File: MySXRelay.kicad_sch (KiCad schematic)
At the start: 53 parts, among them K1 FH44L-1AT-L1-DC5V, Q1 2N7002, U1 MIC4427, U2 BL0942, U3 BP2525X, U4 Si8642BB-B-IS1, U5 MCP1703Ax-180xxTT

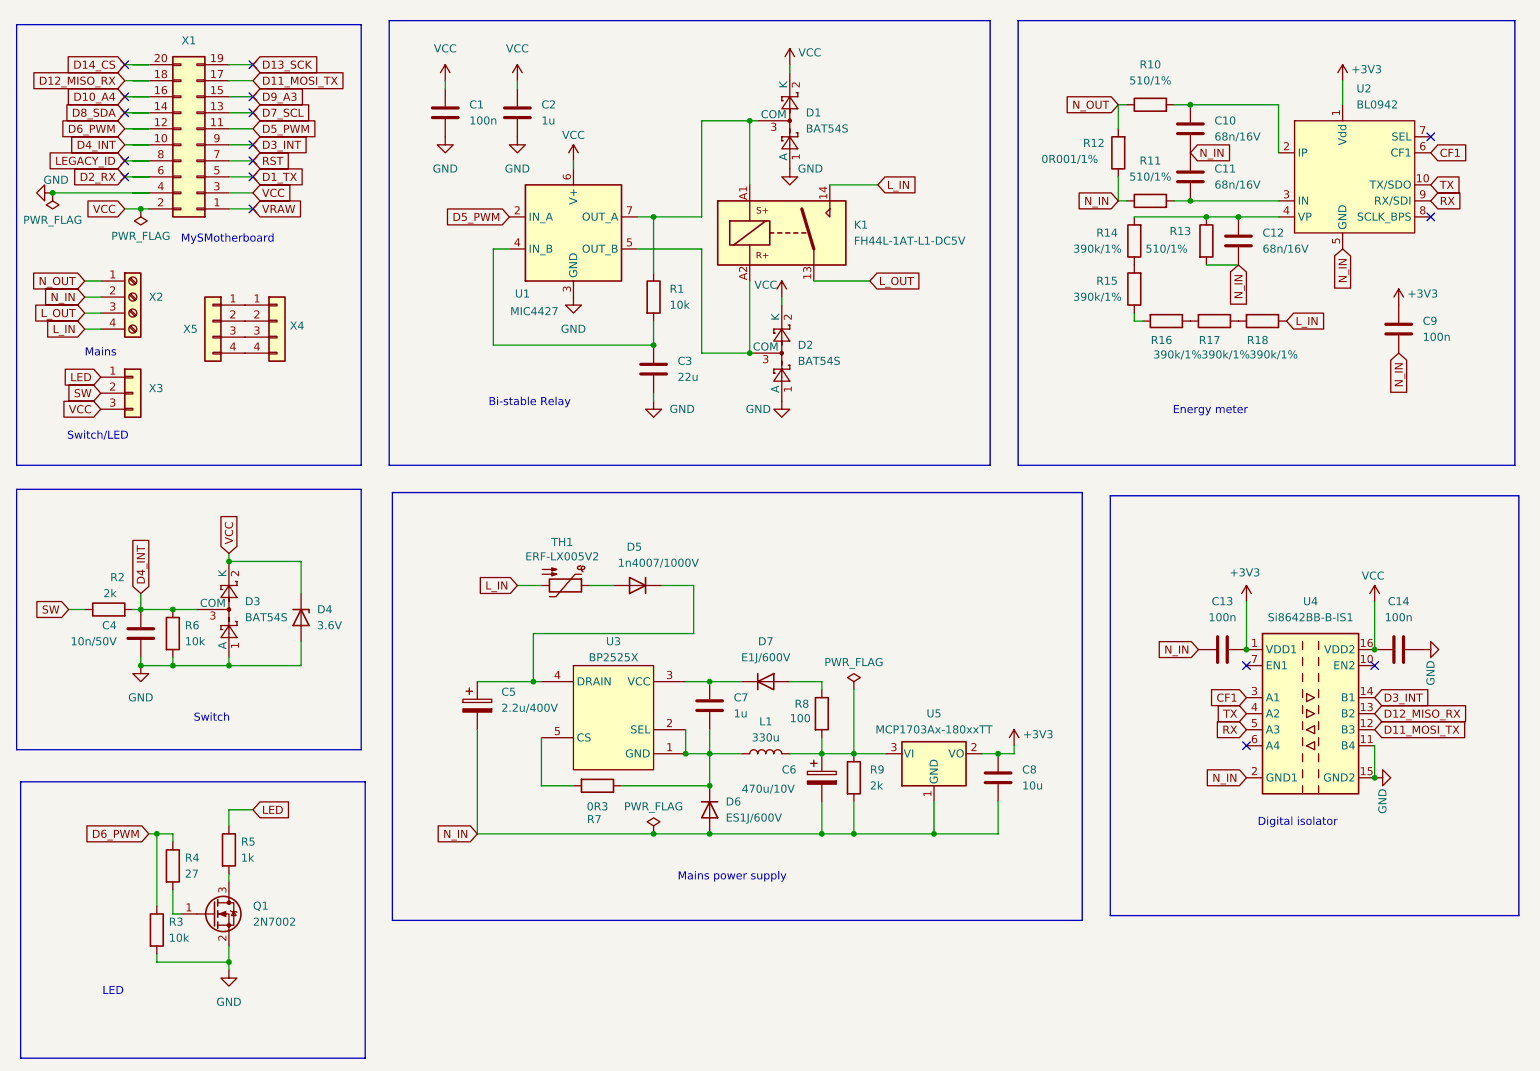
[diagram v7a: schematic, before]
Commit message: update schematic to new version
- include MCU, remove MySXMotherboard
- only RS485 interface is isolated
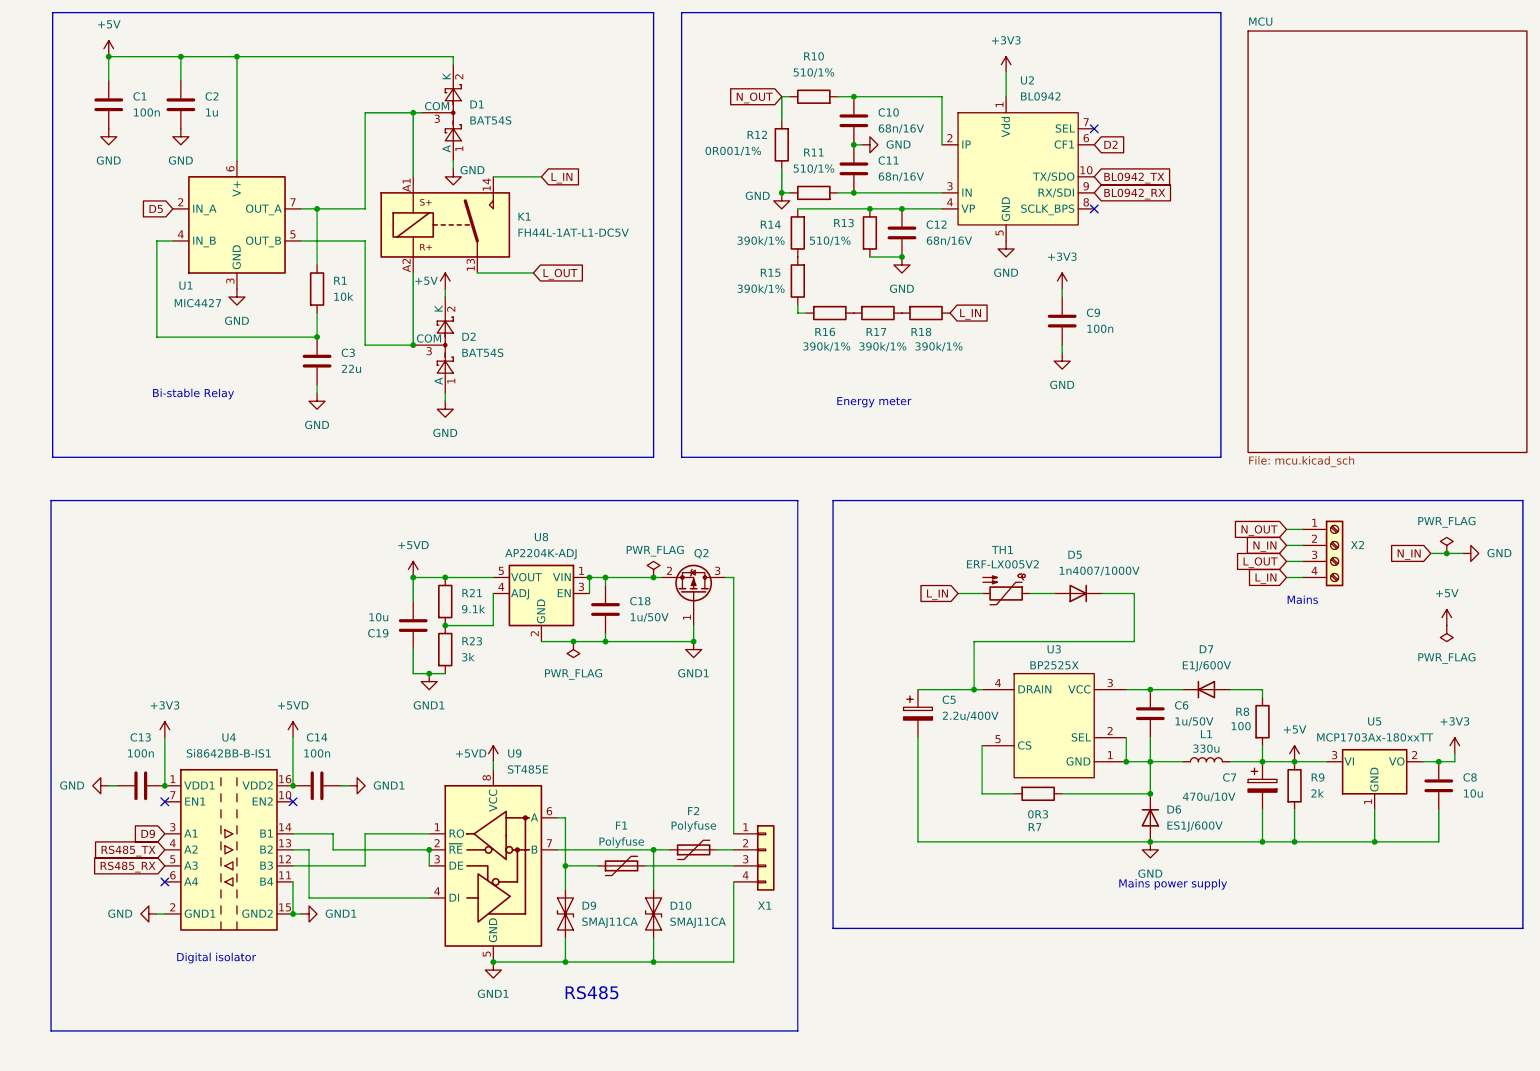
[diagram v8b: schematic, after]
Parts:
- removed C4: 10n/50V, Capacitor_SMD:C_0402_1005Metric, symbol Device:C
- removed C6: 470u/10V, Capacitor_THT:CP_Radial_D8.0mm_P3.50mm, symbol Device:C_Polarized
- removed C7: 1u, Capacitor_SMD:C_0603_1608Metric, symbol Device:C
- removed D3: BAT54S, Package_TO_SOT_SMD:SOT-23, symbol Diode:BAT54S
- removed D4: 3.6V, Diode_SMD:D_MiniMELF, symbol Device:D_Zener
- removed Q1: 2N7002, Package_TO_SOT_SMD:SOT-23, symbol Transistor_FET:2N7002
- removed R2: 2k, Resistor_SMD:R_0603_1608Metric, symbol Device:R
- removed R3, R6: 10k, Resistor_SMD:R_0603_1608Metric, symbol Device:R
- removed R4: 27, Resistor_SMD:R_0603_1608Metric, symbol Device:R
- removed R5: 1k, Resistor_SMD:R_0603_1608Metric, symbol Device:R
- removed X1: ~, Connector_PinSocket_2.54mm:PinSocket_2x10_P2.54mm_Vertical, symbol Connector_Generic:Conn_02x10_Odd_Even
- removed X3: ~, MySXRelay:JST-XH_S_3P-2.54MM, symbol Connector_Generic:Conn_01x03
- removed X4: ~, Connector_PinSocket_2.54mm:PinSocket_1x04_P2.54mm_Vertical, symbol Connector_Generic:Conn_01x04
- removed X5: ~, MySXRelay:JST-XH_S_4P-2.54MM-PIN1-RIGHT, symbol Connector_Generic:Conn_01x04
- added C18, C6: 1u/50V, Capacitor_SMD:C_0603_1608Metric, symbol Device:C
- added C19: 10u, Capacitor_SMD:C_0603_1608Metric, symbol Device:C
- added C7: 470u/10V, Capacitor_THT:CP_Radial_D8.0mm_P3.50mm, symbol Device:C_Polarized
- added D10, D9: SMAJ11CA, Diode_SMD:D_SMA, symbol Diode:SMAJ11CA
- added F1, F2: Polyfuse, Fuse:Fuse_1206_3216Metric_Pad1.42x1.75mm_HandSolder, symbol Device:Polyfuse
- added Q2: ~, Package_TO_SOT_SMD:SOT-23, symbol Device:Q_PMOS_GSD
- added R21: 9.1k, Resistor_SMD:R_0603_1608Metric, symbol Device:R
- added R23: 3k, Resistor_SMD:R_0603_1608Metric, symbol Device:R
- added U8: AP2204K-ADJ, Package_TO_SOT_SMD:SOT-23-5, symbol Regulator_Linear:AP2204K-ADJ
- added U9: ST485E, Package_SO:SOIC-8_3.9x4.9mm_P1.27mm, symbol Interface_UART:ST485E
- added X1: ~, MySXRelay:JST-XH_S_4P-2.54MM-PIN1-RIGHT, symbol Connector_Generic:Conn_01x04
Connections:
- net N_IN is gone; now on net GND: C10.2, C11.1, C12.2, C13.1, C5.2, C8.2, C9.2, D6.2 (A), R11.1, R12.1, R13.2, R9.2, U2.5 (GND), U4.2 (GND1), U4.8 (GND1), U5.1 (GND), X2.2 (Pin_2)
- net GND: now also C7.2; no longer C14.2, U4.11 (B4), U4.15 (GND2), U4.9 (GND2)
- net +5V: now reaches L1.2, R8.2, R9.1, U5.3 (VI)
- net +5V: now also C1.1, C2.1, D1.2 (K), D2.2 (K), U1.6 (V+), C7.1
- net at D7.1 (K), U3.3 (VCC): now also C6.1
- net at D6.1 (K), L1.1, R7.1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: now also C6.2
- net CF1 renamed D2
- net D2: no longer U4.3 (A1)
- net D11_MOSI_TX: no longer names the net of U4.12 (B3)
- net D11_MOSI_TX: now also U9.1 (RO)
- net D12_MISO_RX: no longer names the net of U4.13 (B2)
- net D12_MISO_RX: now also U9.4 (DI)
- net D3_INT: no longer names the net of U4.14 (B1)
- net D3_INT: now also U9.2 (~{RE}), U9.3 (DE)
- net D5_PWM renamed D5
- net RX renamed BL0942_RX
- net BL0942_RX: no longer U4.5 (A3)
- net TX renamed BL0942_TX
- net BL0942_TX: no longer U4.4 (A2)
- removed net VCC: C1.1, C14.1, C2.1, D1.2 (K), D2.2 (K), U1.6 (V+), U4.16 (VDD2)
- new net: C18.1, Q2.2 (S), U8.1 (VIN), U8.3 (EN)
- new net: D9.2 (A2), F1.1, U9.6 (A)
- new net: F1.2, X1.3 (Pin_3)
- new net: D10.2 (A2), F2.1, U9.7 (B)
- new net: F2.2, X1.2 (Pin_2)
- new net: R21.2, R23.1, U8.4 (ADJ)
- new net: Q2.3 (D), X1.1 (Pin_1)
- new net +5VD: C14.1, C19.2, R21.1, U4.16 (VDD2), U8.5 (VOUT), U9.8 (VCC)
- new net D9: U4.3 (A1)
- new net GND1: C14.2, C18.2, C19.1, D10.1 (A1), D9.1 (A1), Q2.1 (G), R23.2, U4.11 (B4), U4.15 (GND2), U4.9 (GND2), U8.2 (GND), U9.5 (GND), X1.4 (Pin_4)
- new net RS485_RX: U4.5 (A3)
- new net RS485_TX: U4.4 (A2)
- no-connect marks 17 -> 5
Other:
- added sheet MCU (mcu.kicad_sch)
- note added: "RS485"
- note removed: "LED"
- note removed: "MySMotherboard"
- note removed: "Switch"
- note removed: "Switch/LED"
- moved on the sheet: C1, C10, C11, C12, C13, C14, C2, C3, C9, D1, D2, K1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
